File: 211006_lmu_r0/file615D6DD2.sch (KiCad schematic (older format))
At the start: 29 parts

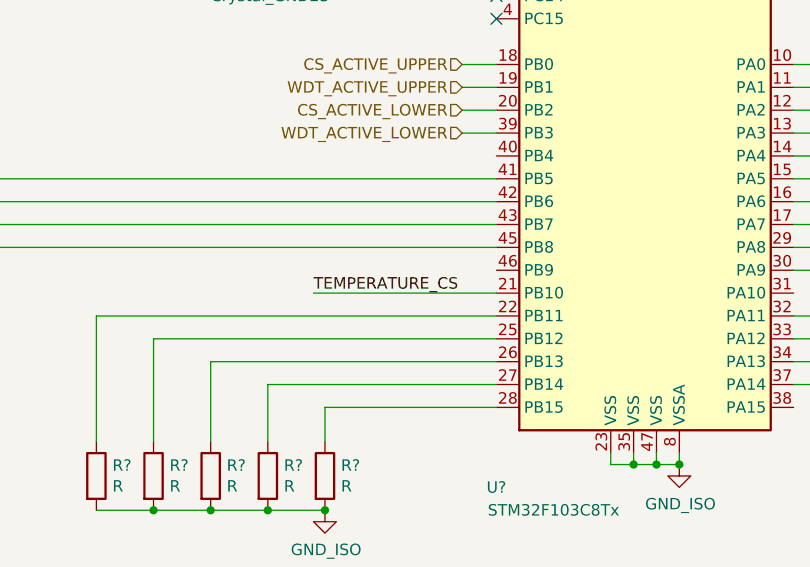
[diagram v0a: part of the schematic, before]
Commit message: inverted logic for the LMS fault detection relay
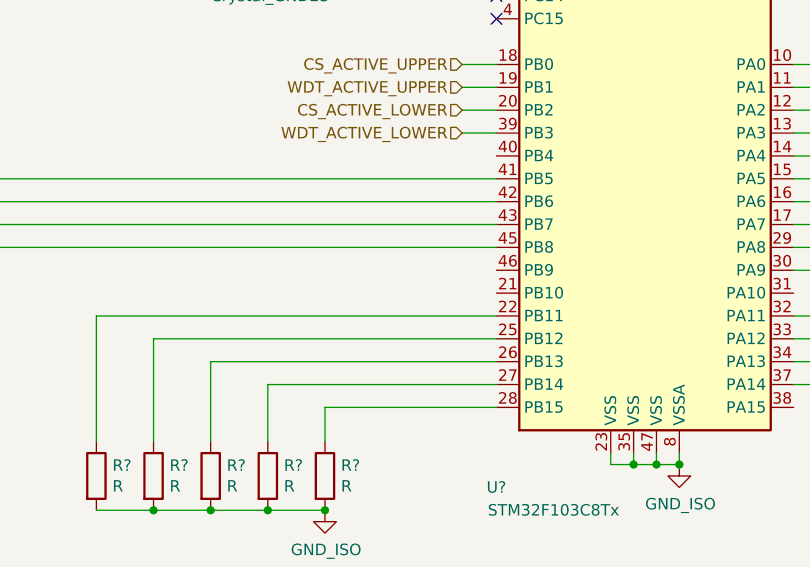
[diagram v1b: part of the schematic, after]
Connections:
- net labels removed: TEMPERATURE_CS
- wire segments 84 -> 83
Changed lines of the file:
@@
 Text HLabel 7400 4400 2    50   Input ~ 0
 SPI1_MOSI
-Text Label 4800 4700 0    50   ~ 0
-TEMPERATURE_CS
-Wire Wire Line
-	4800 4700 5600 4700
 Wire Wire Line
 	1250 2050 1350 2050

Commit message: Updated BOM and footprints for non-hv components
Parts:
- removed C? (x3): C, symbol Device:C
- removed D? (x3): LED, symbol Device:LED
- removed R? (x8): R, symbol Device:R
- added C? (x3): 100n, Capacitor_SMD:C_0603_1608Metric_Pad1.08x0.95mm_HandSolder, symbol Device:C
- added D?: LED (Blue) RX, LED_SMD:LED_0805_2012Metric_Pad1.15x1.40mm_HandSolder, symbol Device:LED
- added D? (x2): LED (Orange), LED_SMD:LED_0805_2012Metric_Pad1.15x1.40mm_HandSolder, symbol Device:LED
- added D?: LED (Red) LED0, LED_SMD:LED_0805_2012Metric_Pad1.15x1.40mm_HandSolder, symbol Device:LED
- added R? (x4): 2.2k, Resistor_SMD:R_0603_1608Metric_Pad0.98x0.95mm_HandSolder, symbol Device:R
- C182: renamed from C?; value C -> 10n; footprint (none) -> Capacitor_SMD:C_0603_1608Metric_Pad1.08x0.95mm_HandSolder
- C183: renamed from C?; value C -> 1u; footprint (none) -> Capacitor_SMD:C_0805_2012Metric_Pad1.18x1.45mm_HandSolder
- D40: renamed from D?; value LED -> LED (Blue) TX; footprint (none) -> LED_SMD:LED_0805_2012Metric_Pad1.15x1.40mm_HandSolder
- FB2: renamed from FB?; footprint (none) -> Inductor_SMD:L_0603_1608Metric_Pad1.05x0.95mm_HandSolder; Manufacturer (none) -> TDK Corportation; Part Number (none) -> MMZ2012Y202BTD25
- J11: renamed from J?; footprint (none) -> Connector_PinHeader_1.27mm:PinHeader_2x09_P1.27mm_Vertical_SMD
- J12: renamed from J?; footprint (none) -> Connector_PinHeader_2.54mm:PinHeader_1x03_P2.54mm_Vertical
- R242: renamed from R?; value R -> 2.2k; footprint (none) -> Resistor_SMD:R_0603_1608Metric_Pad0.98x0.95mm_HandSolder
- R246: renamed from R?; value R -> 50k; footprint (none) -> Resistor_SMD:R_0603_1608Metric_Pad0.98x0.95mm_HandSolder
- SW1: renamed from SW?; footprint (none) -> Button_Switch_SMD:SW_SPST_Omron_B3FS-100xP
- SW2: renamed from SW?; footprint (none) -> Button_Switch_SMD:SW_DIP_SPSTx01_Slide_9.78x4.72mm_W8.61mm_P2.54mm
- gave numbers to parts that had none: 5
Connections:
- wire segments 83 -> 70
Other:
- note added: "Place LC circuit as close as possible to VDDA"

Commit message: Added most footprint requirements in HV
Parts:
- gave numbers to parts that had none: 11
- renumbered FB2 to FB1, R246 to R247, TP8 to TP153, TP9 to TP154, TP10 to TP155
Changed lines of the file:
@@
 $EndDescr
 $Comp
-L Device:Ferrite_Bead FB2
+L Device:Ferrite_Bead FB1
 U 1 1 615D9E48
 P 7050 2400
-F 0 "FB2" V 7200 2450 50  0000 C CNN
+F 0 "FB1" V 7200 2450 50  0000 C CNN
 F 1 "Ferrite_Bead" V 7300 2450 50  0000 C CNN
 F 2 "Inductor_SMD:L_0603_1608Metric_Pad1.05x0.95mm_HandSolder" V 6980 2400 50  0001 C CNN
@@
 $EndComp
 $Comp
-L Device:R R246
+L Device:R R247
 U 1 1 615E3363
 P 3350 2450
-F 0 "R246" H 3420 2496 50  0000 L CNN
+F 0 "R247" H 3420 2496 50  0000 L CNN
 F 1 "50k" H 3420 2405 50  0000 L CNN
 F 2 "Resistor_SMD:R_0603_1608Metric_Pad0.98x0.95mm_HandSolder" V 3280 2450 50  0001 C CNN
@@
 	6900 5100 7400 5100
 $Comp
-L Connector:TestPoint TP8
+L Connector:TestPoint TP153
 U 1 1 616033D7
 P 3000 2600
-F 0 "TP8" H 3058 2718 50  0000 L CNN
+F 0 "TP153" H 3058 2718 50  0000 L CNN
 F 1 "TestPoint" H 3058 2627 50  0000 L CNN
 F 2 "" H 3200 2600 50  0001 C CNN
@@
 	6900 4200 7400 4200
 $Comp
-L Connector:TestPoint TP9
+L Connector:TestPoint TP154
 U 1 1 6162689C
 P 3200 1000
-F 0 "TP9" V 3154 1188 50  0000 L CNN
+F 0 "TP154" V 3154 1188 50  0000 L CNN
 F 1 "TestPoint" V 3245 1188 50  0000 L CNN
 F 2 "" H 3400 1000 50  0001 C CNN
@@
 $EndComp
 $Comp
-L Connector:TestPoint TP10
+L Connector:TestPoint TP155
 U 1 1 6162866E
 P 3200 1100
-F 0 "TP10" V 3154 1288 50  0000 L CNN
+F 0 "TP155" V 3154 1288 50  0000 L CNN
 F 1 "TestPoint" V 3245 1288 50  0000 L CNN
 F 2 "" H 3400 1100 50  0001 C CNN
@@
 LMS_OK_FB
 $Comp
-L gnd_iso:GND_ISO #PWR0177
+L gnd_iso:GND_ISO #PWR090
 U 1 1 6167E3FB
 P 6400 5450
-F 0 "#PWR0177" H 6400 5200 50  0001 C CNN
+F 0 "#PWR090" H 6400 5200 50  0001 C CNN
 F 1 "GND_ISO" H 6405 5277 50  0000 C CNN
 F 2 "" H 6400 5450 50  0001 C CNN
@@
 Connection ~ 6400 5450
 $Comp
-L gnd_iso:GND_ISO #PWR0179
+L gnd_iso:GND_ISO #PWR084
 U 1 1 616863A7
 P 2950 5700
-F 0 "#PWR0179" H 2950 5450 50  0001 C CNN
+F 0 "#PWR084" H 2950 5450 50  0001 C CNN
 F 1 "GND_ISO" H 2955 5527 50  0000 C CNN
 F 2 "" H 2950 5700 50  0001 C CNN
@@
 $EndComp
 $Comp
-L gnd_iso:GND_ISO #PWR0180
+L gnd_iso:GND_ISO #PWR082
 U 1 1 616868B5
 P 2600 5700
-F 0 "#PWR0180" H 2600 5450 50  0001 C CNN
+F 0 "#PWR082" H 2600 5450 50  0001 C CNN
 F 1 "GND_ISO" H 2605 5527 50  0000 C CNN
 F 2 "" H 2600 5700 50  0001 C CNN
@@
 $EndComp
 $Comp
-L gnd_iso:GND_ISO #PWR0181
+L gnd_iso:GND_ISO #PWR081
 U 1 1 61686B7B
 P 2200 5700
-F 0 "#PWR0181" H 2200 5450 50  0001 C CNN
+F 0 "#PWR081" H 2200 5450 50  0001 C CNN
 F 1 "GND_ISO" H 2205 5527 50  0000 C CNN
 F 2 "" H 2200 5700 50  0001 C CNN
@@
 $EndComp
 $Comp
-L gnd_iso:GND_ISO #PWR0182
+L gnd_iso:GND_ISO #PWR079
 U 1 1 61686E61
 P 1800 5700
-F 0 "#PWR0182" H 1800 5450 50  0001 C CNN
+F 0 "#PWR079" H 1800 5450 50  0001 C CNN
 F 1 "GND_ISO" H 1805 5527 50  0000 C CNN
 F 2 "" H 1800 5700 50  0001 C CNN
@@
 $EndComp
 $Comp
-L gnd_iso:GND_ISO #PWR0183
+L gnd_iso:GND_ISO #PWR089
 U 1 1 61687132
 P 4750 3050
-F 0 "#PWR0183" H 4750 2800 50  0001 C CNN
+F 0 "#PWR089" H 4750 2800 50  0001 C CNN
 F 1 "GND_ISO" H 4755 2877 50  0000 C CNN
 F 2 "" H 4750 3050 50  0001 C CNN
@@
 $EndComp
 $Comp
-L gnd_iso:GND_ISO #PWR0184
+L gnd_iso:GND_ISO #PWR088
 U 1 1 61687B4C
 P 4250 3050
-F 0 "#PWR0184" H 4250 2800 50  0001 C CNN
+F 0 "#PWR088" H 4250 2800 50  0001 C CNN
 F 1 "GND_ISO" H 4255 2877 50  0000 C CNN
 F 2 "" H 4250 3050 50  0001 C CNN
@@
 $EndComp
 $Comp
-L gnd_iso:GND_ISO #PWR0185
+L gnd_iso:GND_ISO #PWR086
 U 1 1 61687CD1
 P 3350 3000
-F 0 "#PWR0185" H 3350 2750 50  0001 C CNN
+F 0 "#PWR086" H 3350 2750 50  0001 C CNN
 F 1 "GND_ISO" H 3355 2827 50  0000 C CNN
 F 2 "" H 3350 3000 50  0001 C CNN
@@
 Connection ~ 3350 3000
 $Comp
-L gnd_iso:GND_ISO #PWR0186
+L gnd_iso:GND_ISO #PWR087
 U 1 1 61688149
 P 3750 3200
-F 0 "#PWR0186" H 3750 2950 50  0001 C CNN
+F 0 "#PWR087" H 3750 2950 50  0001 C CNN
 F 1 "GND_ISO" H 3755 3027 50  0000 C CNN
 F 2 "" H 3750 3200 50  0001 C CNN
@@
 	7300 2250 7550 2250
 $Comp
-L gnd_iso:GND_ISO #PWR0187
+L gnd_iso:GND_ISO #PWR091
 U 1 1 6168DF3C
 P 7550 2550
-F 0 "#PWR0187" H 7550 2300 50  0001 C CNN
+F 0 "#PWR091" H 7550 2300 50  0001 C CNN
 F 1 "GND_ISO" H 7555 2377 50  0000 C CNN
 F 2 "" H 7550 2550 50  0001 C CNN
@@
 $EndComp
 $Comp
-L gnd_iso:GND_ISO #PWR0188
+L gnd_iso:GND_ISO #PWR092
 U 1 1 6168E2CF
 P 7900 2550
-F 0 "#PWR0188" H 7900 2300 50  0001 C CNN
+F 0 "#PWR092" H 7900 2300 50  0001 C CNN
 F 1 "GND_ISO" H 7905 2377 50  0000 C CNN
 F 2 "" H 7900 2550 50  0001 C CNN
@@
 $EndComp
 $Comp
-L gnd_iso:GND_ISO #PWR0189
+L gnd_iso:GND_ISO #PWR093
 U 1 1 6168E724
 P 8250 2550
-F 0 "#PWR0189" H 8250 2300 50  0001 C CNN
+F 0 "#PWR093" H 8250 2300 50  0001 C CNN
 F 1 "GND_ISO" H 8255 2377 50  0000 C CNN
 F 2 "" H 8250 2550 50  0001 C CNN
@@
 $EndComp
 $Comp
-L gnd_iso:GND_ISO #PWR0190
+L gnd_iso:GND_ISO #PWR095
 U 1 1 6168E993
 P 8600 2550
-F 0 "#PWR0190" H 8600 2300 50  0001 C CNN
+F 0 "#PWR095" H 8600 2300 50  0001 C CNN
 F 1 "GND_ISO" H 8605 2377 50  0000 C CNN
 F 2 "" H 8600 2550 50  0001 C CNN
@@
 $EndComp
 $Comp
-L gnd_iso:GND_ISO #PWR0191
+L gnd_iso:GND_ISO #PWR078
 U 1 1 6168ECF0
 P 1350 2050
-F 0 "#PWR0191" H 1350 1800 50  0001 C CNN
+F 0 "#PWR078" H 1350 1800 50  0001 C CNN
 F 1 "GND_ISO" H 1355 1877 50  0000 C CNN
 F 2 "" H 1350 2050 50  0001 C CNN
@@
 Connection ~ 1350 2050
 $Comp
-L gnd_iso:GND_ISO #PWR0192
+L gnd_iso:GND_ISO #PWR083
 U 1 1 6168F039
 P 2800 1200
-F 0 "#PWR0192" H 2800 950 50  0001 C CNN
+F 0 "#PWR083" H 2800 950 50  0001 C CNN
 F 1 "GND_ISO" H 2805 1027 50  0000 C CNN
 F 2 "" H 2800 1200 50  0001 C CNN
@@
 $EndComp
 $Comp
-L +3v3_iso:+3V3_ISO #PWR0193
+L +3v3_iso:+3V3_ISO #PWR094
 U 1 1 6168FEF9
 P 8600 2250
-F 0 "#PWR0193" H 8600 2100 50  0001 C CNN
+F 0 "#PWR094" H 8600 2100 50  0001 C CNN
 F 1 "+3V3_ISO" H 8850 2300 50  0000 C CNN
 F 2 "" H 8600 2250 50  0001 C CNN
@@
 $EndComp
 $Comp
-L +3v3_iso:+3V3_ISO #PWR0194
+L +3v3_iso:+3V3_ISO #PWR085
 U 1 1 61692F23
 P 3350 2300
-F 0 "#PWR0194" H 3350 2150 50  0001 C CNN
+F 0 "#PWR085" H 3350 2150 50  0001 C CNN
 F 1 "+3V3_ISO" H 3365 2473 50  0000 C CNN
 F 2 "" H 3350 2300 50  0001 C CNN
@@
 $EndComp
 $Comp
-L +3v3_iso:+3V3_ISO #PWR0195
+L +3v3_iso:+3V3_ISO #PWR077
 U 1 1 616935BF
 P 1350 850
-F 0 "#PWR0195" H 1350 700 50  0001 C CNN
+F 0 "#PWR077" H 1350 700 50  0001 C CNN
 F 1 "+3V3_ISO" H 1365 1023 50  0000 C CNN
 F 2 "" H 1350 850 50  0001 C CNN
@@
 	7550 2250 7900 2250
 $Comp
-L Device:C C?
+L Device:C C184
 U 1 1 61F50BE3
 P 7900 2400
-F 0 "C?" H 7800 2800 50  0000 L CNN
+F 0 "C184" H 7800 2800 50  0000 L CNN
 F 1 "100n" H 7800 2700 50  0000 L CNN
 F 2 "Capacitor_SMD:C_0603_1608Metric_Pad1.08x0.95mm_HandSolder" H 7938 2250 50  0001 C CNN
@@
 	7900 2250 8250 2250
 $Comp
-L Device:C C?
+L Device:C C185
 U 1 1 61F50E1A
 P 8250 2400
-F 0 "C?" H 8150 2800 50  0000 L CNN
+F 0 "C185" H 8150 2800 50  0000 L CNN
 F 1 "100n" H 8150 2700 50  0000 L CNN
 F 2 "Capacitor_SMD:C_0603_1608Metric_Pad1.08x0.95mm_HandSolder" H 8288 2250 50  0001 C CNN
@@
 	8250 2250 8600 2250
 $Comp
-L Device:C C?
+L Device:C C186
 U 1 1 61F510EB
 P 8600 2400
-F 0 "C?" H 8500 2800 50  0000 L CNN
+F 0 "C186" H 8500 2800 50  0000 L CNN
 F 1 "100n" H 8500 2700 50  0000 L CNN
 F 2 "Capacitor_SMD:C_0603_1608Metric_Pad1.08x0.95mm_HandSolder" H 8638 2250 50  0001 C CNN
@@
 Place LC circuit as close as possible to VDDA
 $Comp
-L Device:R R?
+L Device:R R244
 U 1 1 61F577D6
 P 2200 5250
-F 0 "R?" H 2270 5296 50  0000 L CNN
+F 0 "R244" H 2270 5296 50  0000 L CNN
 F 1 "2.2k" H 2270 5205 50  0000 L CNN
 F 2 "Resistor_SMD:R_0603_1608Metric_Pad0.98x0.95mm_HandSolder" V 2130 5250 50  0001 C CNN
@@
 $EndComp
 $Comp
-L Device:R R?
+L Device:R R245
 U 1 1 61F57A93
 P 2600 5250
-F 0 "R?" H 2670 5296 50  0000 L CNN
+F 0 "R245" H 2670 5296 50  0000 L CNN
 F 1 "2.2k" H 2670 5205 50  0000 L CNN
 F 2 "Resistor_SMD:R_0603_1608Metric_Pad0.98x0.95mm_HandSolder" V 2530 5250 50  0001 C CNN
@@
 $EndComp
 $Comp
-L Device:R R?
+L Device:R R246
 U 1 1 61F57D63
 P 2950 5250
-F 0 "R?" H 3020 5296 50  0000 L CNN
+F 0 "R246" H 3020 5296 50  0000 L CNN
 F 1 "2.2k" H 3020 5205 50  0000 L CNN
 F 2 "Resistor_SMD:R_0603_1608Metric_Pad0.98x0.95mm_HandSolder" V 2880 5250 50  0001 C CNN
@@
 $EndComp
 $Comp
-L Device:LED D?
+L Device:LED D42
 U 1 1 61F583AC
 P 2200 5550
-F 0 "D?" V 1750 5900 50  0000 R CNN
+F 0 "D42" V 1750 5900 50  0000 R CNN
 F 1 "LED (Blue) RX" V 1650 5900 50  0000 R CNN
 F 2 "LED_SMD:LED_0805_2012Metric_Pad1.15x1.40mm_HandSolder" H 2200 5550 50  0001 C CNN
@@
 $EndComp
 $Comp
-L Device:LED D?
+L Device:LED D43
 U 1 1 61F58EEB
 P 2600 5550
-F 0 "D?" V 2150 5600 50  0000 R CNN
+F 0 "D43" V 2150 5600 50  0000 R CNN
 F 1 "LED (Orange)" V 2050 5600 50  0000 R CNN
 F 2 "LED_SMD:LED_0805_2012Metric_Pad1.15x1.40mm_HandSolder" H 2600 5550 50  0001 C CNN
@@
 $EndComp
 $Comp
-L Device:LED D?
+L Device:LED D44
 U 1 1 61F594E6
 P 2950 5550
-F 0 "D?" V 2500 5350 50  0000 R CNN
+F 0 "D44" V 2500 5350 50  0000 R CNN
 F 1 "LED (Orange)" V 2400 5350 50  0000 R CNN
 F 2 "LED_SMD:LED_0805_2012Metric_Pad1.15x1.40mm_HandSolder" H 2950 5550 50  0001 C CNN
@@
 LED0
 $Comp
-L Device:R R?
+L Device:R R243
 U 1 1 61F59B9C
 P 1850 3350
-F 0 "R?" H 1920 3396 50  0000 L CNN
+F 0 "R243" H 1920 3396 50  0000 L CNN
 F 1 "2.2k" H 1920 3305 50  0000 L CNN
 F 2 "Resistor_SMD:R_0603_1608Metric_Pad0.98x0.95mm_HandSolder" V 1780 3350 50  0001 C CNN
@@
 $EndComp
 $Comp
-L Device:LED D?
+L Device:LED D41
 U 1 1 61F59EAA
 P 1850 3650
-F 0 "D?" V 1850 4350 50  0000 R CNN
+F 0 "D41" V 1850 4350 50  0000 R CNN
 F 1 "LED (Red) LED0" V 1750 4350 50  0000 R CNN
 F 2 "LED_SMD:LED_0805_2012Metric_Pad1.15x1.40mm_HandSolder" H 1850 3650 50  0001 C CNN
@@
 $EndComp
 $Comp
-L gnd_iso:GND_ISO #PWR?
+L gnd_iso:GND_ISO #PWR080
 U 1 1 61F5A303
 P 1850 3800
-F 0 "#PWR?" H 1850 3550 50  0001 C CNN
+F 0 "#PWR080" H 1850 3550 50  0001 C CNN
 F 1 "GND_ISO" H 1855 3627 50  0000 C CNN
 F 2 "" H 1850 3800 50  0001 C CNN

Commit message: Cleaned up last components missing footprint refs
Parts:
- TP153, TP154, TP155: footprint (none) -> TestPoint:TestPoint_Pad_D1.0mm
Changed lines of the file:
@@
 F 0 "TP153" H 3058 2718 50  0000 L CNN
 F 1 "TestPoint" H 3058 2627 50  0000 L CNN
-F 2 "" H 3200 2600 50  0001 C CNN
+F 2 "TestPoint:TestPoint_Pad_D1.0mm" H 3200 2600 50  0001 C CNN
 F 3 "~" H 3200 2600 50  0001 C CNN
 	1    3000 2600
@@
 F 0 "TP154" V 3154 1188 50  0000 L CNN
 F 1 "TestPoint" V 3245 1188 50  0000 L CNN
-F 2 "" H 3400 1000 50  0001 C CNN
+F 2 "TestPoint:TestPoint_Pad_D1.0mm" H 3400 1000 50  0001 C CNN
 F 3 "~" H 3400 1000 50  0001 C CNN
 	1    3200 1000
@@
 F 0 "TP155" V 3154 1288 50  0000 L CNN
 F 1 "TestPoint" V 3245 1288 50  0000 L CNN
-F 2 "" H 3400 1100 50  0001 C CNN
+F 2 "TestPoint:TestPoint_Pad_D1.0mm" H 3400 1100 50  0001 C CNN
 F 3 "~" H 3400 1100 50  0001 C CNN
 	1    3200 1100
